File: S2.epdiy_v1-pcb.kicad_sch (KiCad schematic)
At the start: 80 parts, among them J1 USB_C_Receptacle_USB2.0, J2 Jack-DC, P1 CONN_02X13, SW1 RESET, SW2 BOOT, U1 MCP1700-1202E_SOT23, U11 TP4056, U2 ESP32-S2-WROVER, U3 TPS651851RSLR, U6 ED060XC5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

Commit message: DRC passes
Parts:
- added H1, H2, H3, H4: MountingHole, MountingHole:MountingHole_2.5mm, symbol Mechanical:MountingHole
- U3: value TPS651851RSLR -> QFN50P700X700X100-49N; footprint footprint:TPS651851RSLR -> footprint:TPS65185RGZR_700X700X100-49N
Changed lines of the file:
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@@
       (effects (font (size 1.524 1.524)))
     )
-    (property "Value" "TPS651851RSLR" (id 1) (at 290.83 147.8026 0)
+    (property "Value" "QFN50P700X700X100-49N" (id 1) (at 290.83 147.8026 0)
       (effects (font (size 1.524 1.524)))
     )
-    (property "Footprint" "footprint:TPS651851RSLR" (id 2) (at 276.86 148.844 0)
+    (property "Footprint" "footprint:TPS65185RGZR_700X700X100-49N" (id 2) (at 276.86 148.844 0)
       (effects (font (size 1.524 1.524)) hide)
     )
@@
     (pin "9")
   )
+  (symbol (lib_id "Mechanical:MountingHole") (at 246.38 260.35 0) (unit 1)
+    (in_bom yes) (on_board yes) (fields_autoplaced)
+    (property "Reference" "H4" (id 0) (at 248.92 259.4415 0)
+      (effects (font (size 1.27 1.27)) (justify left))
+    )
+    (property "Value" "MountingHole" (id 1) (at 248.92 262.2166 0)
+      (effects (font (size 1.27 1.27)) (justify left))
+    )
+    (property "Footprint" "MountingHole:MountingHole_2.5mm" (id 2) (at 246.38 260.35 0)
+      (effects (font (size 1.27 1.27)) hide)
+    )
+    (property "Datasheet" "~" (id 3) (at 246.38 260.35 0)
+      (effects (font (size 1.27 1.27)) hide)
+    )
+  )
   (symbol (lib_id "Device:R") (at 80.01 40.64 270) (unit 1)
     (in_bom yes) (on_board yes)
@@
     (pin "1")
   )
+  (symbol (lib_id "Mechanical:MountingHole") (at 228.6 260.35 0) (unit 1)
+    (in_bom yes) (on_board yes) (fields_autoplaced)
+    (property "Reference" "H2" (id 0) (at 231.14 259.4415 0)
+      (effects (font (size 1.27 1.27)) (justify left))
+    )
+    (property "Value" "MountingHole" (id 1) (at 231.14 262.2166 0)
+      (effects (font (size 1.27 1.27)) (justify left))
+    )
+    (property "Footprint" "MountingHole:MountingHole_2.5mm" (id 2) (at 228.6 260.35 0)
+      (effects (font (size 1.27 1.27)) hide)
+    )
+    (property "Datasheet" "~" (id 3) (at 228.6 260.35 0)
+      (effects (font (size 1.27 1.27)) hide)
+    )
+  )
   (symbol (lib_id "Device:R") (at 334.01 82.55 0) (unit 1)
     (in_bom yes) (on_board yes) (fields_autoplaced)
@@
     (pin "1")
     (pin "2")
+  )
+  (symbol (lib_id "Mechanical:MountingHole") (at 228.6 255.27 0) (unit 1)
+    (in_bom yes) (on_board yes) (fields_autoplaced)
+    (property "Reference" "H1" (id 0) (at 231.14 254.3615 0)
+      (effects (font (size 1.27 1.27)) (justify left))
+    )
+    (property "Value" "MountingHole" (id 1) (at 231.14 257.1366 0)
+      (effects (font (size 1.27 1.27)) (justify left))
+    )
+    (property "Footprint" "MountingHole:MountingHole_2.5mm" (id 2) (at 228.6 255.27 0)
+      (effects (font (size 1.27 1.27)) hide)
+    )
+    (property "Datasheet" "~" (id 3) (at 228.6 255.27 0)
+      (effects (font (size 1.27 1.27)) hide)
+    )
+  )
+  (symbol (lib_id "Mechanical:MountingHole") (at 246.38 255.27 0) (unit 1)
+    (in_bom yes) (on_board yes) (fields_autoplaced)
+    (property "Reference" "H3" (id 0) (at 248.92 254.3615 0)
+      (effects (font (size 1.27 1.27)) (justify left))
+    )
+    (property "Value" "MountingHole" (id 1) (at 248.92 257.1366 0)
+      (effects (font (size 1.27 1.27)) (justify left))
+    )
+    (property "Footprint" "MountingHole:MountingHole_2.5mm" (id 2) (at 246.38 255.27 0)
+      (effects (font (size 1.27 1.27)) hide)
+    )
+    (property "Datasheet" "~" (id 3) (at 246.38 255.27 0)
+      (effects (font (size 1.27 1.27)) hide)
+    )
   )
   (symbol (lib_id "Device:C") (at 325.12 53.34 180) (unit 1)
@@
       (reference "D9") (unit 1) (value "RED") (footprint "LED_SMD:LED_0805_2012Metric")
     )
+    (path "/c17299c3-8f60-4082-9be0-bbabc66e38fd"
+      (reference "H1") (unit 1) (value "MountingHole") (footprint "MountingHole:MountingHole_2.5mm")
+    )
+    (path "/ad47bbf2-3f06-4e1b-a037-d0ec556dc5e1"
+      (reference "H2") (unit 1) (value "MountingHole") (footprint "MountingHole:MountingHole_2.5mm")
+    )
+    (path "/c31da7ac-0e84-49c9-a671-1085a8d3b053"
+      (reference "H3") (unit 1) (value "MountingHole") (footprint "MountingHole:MountingHole_2.5mm")
+    )
+    (path "/693f52c8-d32f-4dba-8081-49f9b563b51a"
+      (reference "H4") (unit 1) (value "MountingHole") (footprint "MountingHole:MountingHole_2.5mm")
+    )
     (path "/a74e1b96-4789-49e0-832a-03b096a8ecaa"
       (reference "J1") (unit 1) (value "USB_C_Receptacle_USB2.0") (footprint "footprint:USB_C_Receptacle_HRO_TYPE-C-31-M-12")
@@
     )
     (path "/00000000-0000-0000-0000-0000607396d1"
-      (reference "U3") (unit 1) (value "TPS651851RSLR") (footprint "footprint:TPS651851RSLR")
+      (reference "U3") (unit 1) (value "QFN50P700X700X100-49N") (footprint "footprint:TPS65185RGZR_700X700X100-49N")
     )
     (path "/00000000-0000-0000-0000-000061320af7"

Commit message: Passes DRC
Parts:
- added TP33: TestPoint, TestPoint:TestPoint_Pad_2.0x2.0mm, symbol Connector:TestPoint
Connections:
- net EPD_VDD: now also TP33.1
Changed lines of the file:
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@@
   (junction (at 321.31 232.41) (diameter 0) (color 0 0 0 0)
   )
+  (junction (at 360.68 161.29) (diameter 0) (color 0 0 0 0)
+  )
   (no_connect (at 378.46 41.91))
   (no_connect (at 102.87 138.43))
@@
     (stroke (width 0) (type default) (color 0 0 0 0))
   )
+  (wire (pts (xy 360.68 161.29) (xy 312.42 161.29))
+    (stroke (width 0) (type default) (color 0 0 0 0))
+  )
   (wire (pts (xy 151.13 210.82) (xy 144.78 210.82))
     (stroke (width 0) (type default) (color 0 0 0 0))
@@
     (stroke (width 0) (type default) (color 0 0 0 0))
   )
+  (wire (pts (xy 312.42 162.56) (xy 300.99 162.56))
+    (stroke (width 0) (type default) (color 0 0 0 0))
+  )
   (wire (pts (xy 250.19 200.66) (xy 243.84 200.66))
     (stroke (width 0) (type default) (color 0 0 0 0))
@@
     (stroke (width 0) (type default) (color 0 0 0 0))
   )
+  (wire (pts (xy 361.95 161.29) (xy 360.68 161.29))
+    (stroke (width 0) (type default) (color 0 0 0 0))
+  )
   (wire (pts (xy 300.99 157.48) (xy 308.61 157.48))
     (stroke (width 0) (type default) (color 0 0 0 0))
@@
     (stroke (width 0) (type default) (color 0 0 0 0))
   )
+  (wire (pts (xy 312.42 161.29) (xy 312.42 162.56))
+    (stroke (width 0) (type default) (color 0 0 0 0))
+  )
   (wire (pts (xy 331.47 41.91) (xy 331.47 49.53))
     (stroke (width 0) (type default) (color 0 0 0 0))
@@
     (effects (font (size 1.27 1.27)) (justify right bottom))
   )
-  (global_label "EPD_VDD" (shape input) (at 300.99 162.56 0) (fields_autoplaced)
+  (global_label "EPD_VDD" (shape input) (at 361.95 161.29 0) (fields_autoplaced)
     (effects (font (size 1.27 1.27)) (justify left))
-    (property "Intersheet References" "${INTERSHEET_REFS}" (id 0) (at -34.29 0 0)
+    (property "Intersheet References" "${INTERSHEET_REFS}" (id 0) (at 26.67 -1.27 0)
       (effects (font (size 1.27 1.27)) hide)
     )
@@
     (pin "9")
   )
+  (symbol (lib_id "Connector:TestPoint") (at 360.68 161.29 0) (unit 1)
+    (in_bom yes) (on_board yes)
+    (property "Reference" "TP33" (id 0) (at 359.41 156.21 0)
+      (effects (font (size 1.27 1.27)) (justify left))
+    )
+    (property "Value" "TestPoint" (id 1) (at 363.22 156.21 0)
+      (effects (font (size 1.27 1.27)) (justify left))
+    )
+    (property "Footprint" "TestPoint:TestPoint_Pad_2.0x2.0mm" (id 2) (at 365.76 161.29 0)
+      (effects (font (size 1.27 1.27)) hide)
+    )
+    (property "Datasheet" "~" (id 3) (at 365.76 161.29 0)
+      (effects (font (size 1.27 1.27)) hide)
+    )
+    (pin "1")
+  )
   (symbol (lib_id "Device:LED") (at 326.39 74.93 90) (unit 1)
     (in_bom yes) (on_board yes) (fields_autoplaced)
@@
       (reference "TP5") (unit 1) (value "VCOM") (footprint "TestPoint:TestPoint_Pad_D2.5mm")
     )
+    (path "/de954fc5-54aa-4912-850f-059c315d7062"
+      (reference "TP33") (unit 1) (value "TestPoint") (footprint "TestPoint:TestPoint_Pad_2.0x2.0mm")
+    )
     (path "/6f2dad6e-4f7a-4655-bd41-70ba0551820e"

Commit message: LCSC
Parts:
- C14: LCSC (none) -> C28323
- D8: LCSC (none) -> C2297
- D9: LCSC (none) -> C84256
- R2, R3: value 1K -> 2K2; LCSC (none) -> C25804
- R6, R7: LCSC (none) -> C25803
- SW2: LCSC (none) -> C202388
- U11: LCSC (none) -> C16581
- U2: LCSC (none) -> C701333
- U7: value TPS2113APW -> TPS2113APWR; LCSC (none) -> C130052
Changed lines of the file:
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@@
+      (effects (font (size 1.27 1.27)) hide)
+    )
+    (property "LCSC" "C84256" (id 4) (at 334.01 74.93 90)
       (effects (font (size 1.27 1.27)) hide)
     )
@@
       (effects (font (size 1.524 1.524)))
     )
-    (property "Value" "TPS2113APW" (id 1) (at 360.68 30.5235 0)
+    (property "Value" "TPS2113APWR" (id 1) (at 360.68 30.5235 0)
       (effects (font (size 1.524 1.524)))
     )
@@
     (property "Datasheet" "" (id 3) (at 360.68 44.45 0)
       (effects (font (size 1.524 1.524)))
+    )
+    (property "LCSC" "C130052" (id 4) (at 360.68 44.45 0)
+      (effects (font (size 1.27 1.27)) hide)
     )
     (pin "1")
@@
       (effects (font (size 1.27 1.27)) hide)
     )
+    (property "LCSC" "C28323" (id 4) (at 229.87 49.53 0)
+      (effects (font (size 1.27 1.27)) hide)
+    )
     (pin "1")
     (pin "2")
@@
     )
     (property "Datasheet" "https://www.espressif.com/sites/default/files/documentation/esp32-s2-wroom_esp32-s2-wroom-i_datasheet_en.pdf" (id 3) (at 139.7 45.72 0)
+      (effects (font (size 1.27 1.27)) hide)
+    )
+    (property "LCSC" "C701333" (id 4) (at 132.08 66.04 0)
       (effects (font (size 1.27 1.27)) hide)
     )
@@
       (effects (font (size 1.27 1.27)) hide)
     )
+    (property "LCSC" "C25803" (id 4) (at 80.01 40.64 90)
+      (effects (font (size 1.27 1.27)) hide)
+    )
     (pin "1")
     (pin "2")
@@
       (effects (font (size 1.27 1.27)) (justify left))
     )
-    (property "Value" "1K" (id 1) (at 335.788 84.4166 0)
+    (property "Value" "2K2" (id 1) (at 335.788 84.4166 0)
       (effects (font (size 1.27 1.27)) (justify left))
     )
@@
     )
     (property "Datasheet" "~" (id 3) (at 334.01 82.55 0)
+      (effects (font (size 1.27 1.27)) hide)
+    )
+    (property "LCSC" "C25804" (id 4) (at 334.01 82.55 0)
       (effects (font (size 1.27 1.27)) hide)
     )
@@
     (property "Datasheet" "" (id 3) (at 361.95 85.09 0)
       (effects (font (size 1.524 1.524)))
+    )
+    (property "LCSC" "C16581" (id 4) (at 361.95 85.09 0)
+      (effects (font (size 1.27 1.27)) hide)
     )
     (pin "1")
@@
       (effects (font (size 1.27 1.27)) hide)
     )
+    (property "LCSC" "C2297" (id 4) (at 326.39 74.93 90)
+      (effects (font (size 1.27 1.27)) hide)
+    )
     (pin "1")
     (pin "2")
@@
       (effects (font (size 1.27 1.27)) hide)
     )
-    (property "Datasheet" "~" (id 3) (at 237.49 36.83 0)
+    (property "Datasheet" "" (id 3) (at 237.49 36.83 0)
+      (effects (font (size 1.27 1.27)) hide)
+    )
+    (property "LCSC" "C202388" (id 4) (at 237.49 41.91 0)
       (effects (font (size 1.27 1.27)) hide)
     )
@@
       (effects (font (size 1.27 1.27)) hide)
     )
+    (property "LCSC" "C25803" (id 4) (at 80.01 43.18 90)
+      (effects (font (size 1.27 1.27)) hide)
+    )
     (pin "1")
     (pin "2")
@@
       (effects (font (size 1.27 1.27)) (justify left))
     )
-    (property "Value" "1K" (id 1) (at 328.168 84.4166 0)
+    (property "Value" "2K2" (id 1) (at 328.168 84.4166 0)
       (effects (font (size 1.27 1.27)) (justify left))
     )
@@
     )
     (property "Datasheet" "~" (id 3) (at 326.39 82.55 0)
+      (effects (font (size 1.27 1.27)) hide)
+    )
+    (property "LCSC" "C25804" (id 4) (at 326.39 82.55 0)
       (effects (font (size 1.27 1.27)) hide)
     )
@@
     )
     (path "/f7be12b1-ea68-4680-ba6e-0b0986167f39"
-      (reference "R2") (unit 1) (value "1K") (footprint "Resistor_SMD:R_0603_1608Metric")
+      (reference "R2") (unit 1) (value "2K2") (footprint "Resistor_SMD:R_0603_1608Metric")
     )
     (path "/b392c915-b843-4114-8bca-8feaa4d154f9"
-      (reference "R3") (unit 1) (value "1K") (footprint "Resistor_SMD:R_0603_1608Metric")
+      (reference "R3") (unit 1) (value "2K2") (footprint "Resistor_SMD:R_0603_1608Metric")
     )
     (path "/468ff6b2-84c2-4c8f-aa2b-40a098fd4368"
@@
     )
     (path "/38a48d5e-8f90-4cde-a529-54b3116299fc"
-      (reference "U7") (unit 1) (value "TPS2113APW") (footprint "footprint:TPS2113APW")
+      (reference "U7") (unit 1) (value "TPS2113APWR") (footprint "footprint:TPS2113APW")
     )
     (path "/db763171-2d21-4254-a43f-5acafccd52ae"

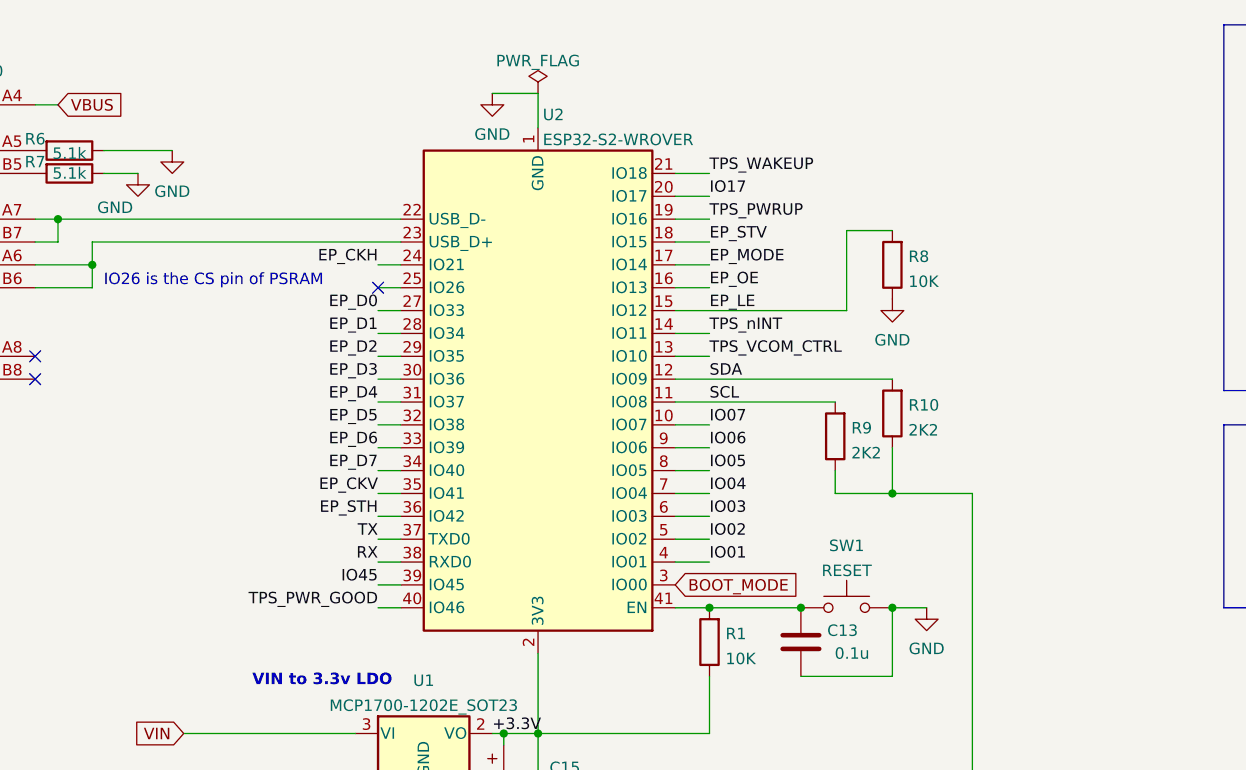
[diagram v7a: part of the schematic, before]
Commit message: 16 VNEG_IN was not connected properly
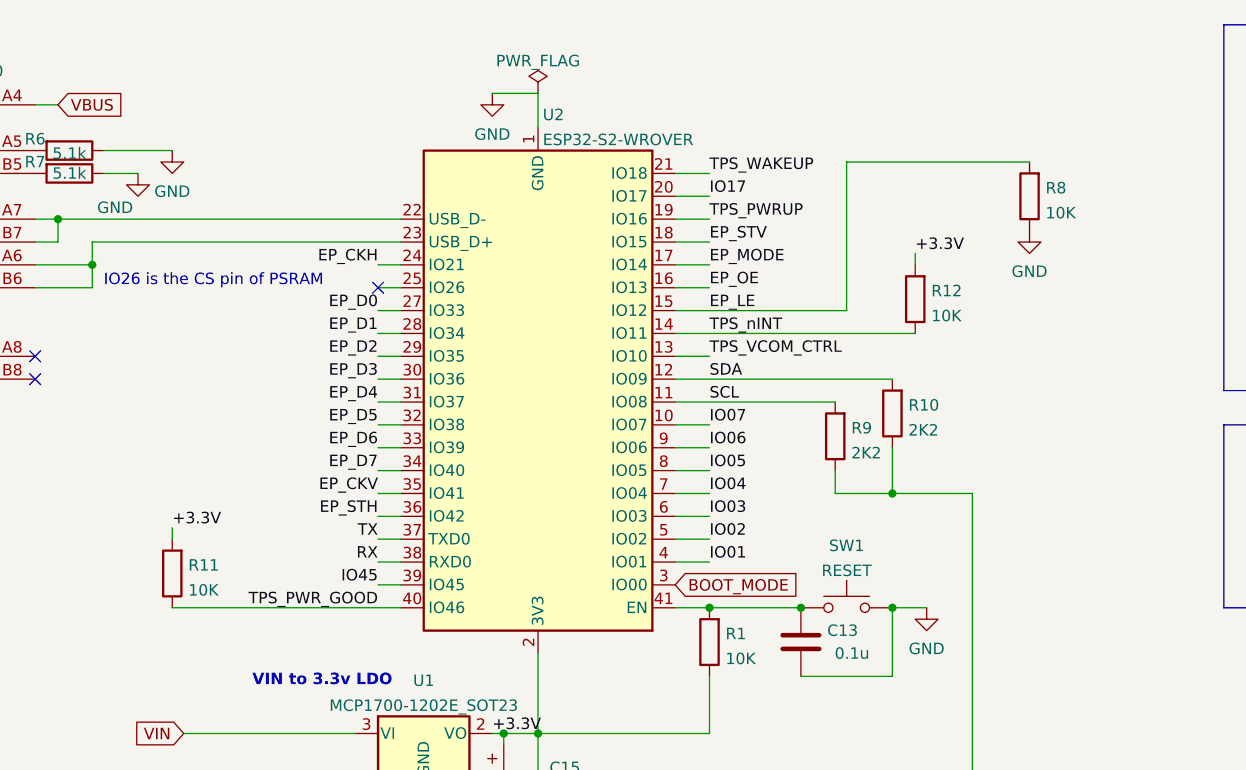
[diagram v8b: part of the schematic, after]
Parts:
- added R11, R12: 10K, Resistor_SMD:R_0603_1608Metric, symbol Device:R
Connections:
- net +3.3V: now also R11.2, R12.2
- net TPS_PWR_GOOD: now also R11.1
- net TPS_nINT: now also R12.1
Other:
- moved on the sheet: R8
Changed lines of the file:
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@@
     (stroke (width 0) (type default) (color 0 0 0 0))
   )
+  (wire (pts (xy 173.99 52.07) (xy 173.99 53.34))
+    (stroke (width 0) (type default) (color 0 0 0 0))
+  )
   (wire (pts (xy 151.13 105.41) (xy 132.08 105.41))
     (stroke (width 0) (type default) (color 0 0 0 0))
@@
     (stroke (width 0) (type default) (color 0 0 0 0))
   )
-  (wire (pts (xy 166.37 58.42) (xy 166.37 49.53))
+  (wire (pts (xy 166.37 58.42) (xy 166.37 41.91))
     (stroke (width 0) (type default) (color 0 0 0 0))
   )
@@
     (stroke (width 0) (type default) (color 0 0 0 0))
   )
-  (wire (pts (xy 151.13 60.96) (xy 147.32 60.96))
+  (wire (pts (xy 147.32 60.96) (xy 173.99 60.96))
     (stroke (width 0) (type default) (color 0 0 0 0))
   )
@@
     (stroke (width 0) (type default) (color 0 0 0 0))
   )
+  (wire (pts (xy 91.44 82.55) (xy 91.44 83.82))
+    (stroke (width 0) (type default) (color 0 0 0 0))
+  )
   (wire (pts (xy 311.15 191.77) (xy 351.79 191.77))
     (stroke (width 0) (type default) (color 0 0 0 0))
@@
     (stroke (width 0) (type default) (color 0 0 0 0))
   )
-  (wire (pts (xy 166.37 49.53) (xy 171.45 49.53))
+  (wire (pts (xy 166.37 41.91) (xy 186.69 41.91))
     (stroke (width 0) (type default) (color 0 0 0 0))
   )
@@
     (stroke (width 0) (type default) (color 0 0 0 0))
   )
-  (wire (pts (xy 114.3 91.44) (xy 116.84 91.44))
+  (wire (pts (xy 91.44 91.44) (xy 116.84 91.44))
     (stroke (width 0) (type default) (color 0 0 0 0))
   )
@@
     (effects (font (size 1.27 1.27)) (justify left bottom))
   )
+  (label "+3.3V" (at 91.44 82.55 0)
+    (effects (font (size 1.27 1.27)) (justify left bottom))
+  )
   (label "TPS_nINT" (at 151.13 60.96 0)
     (effects (font (size 1.27 1.27)) (justify left bottom))
@@
     (effects (font (size 1.27 1.27)) (justify left bottom))
   )
+  (label "+3.3V" (at 173.99 52.07 0)
+    (effects (font (size 1.27 1.27)) (justify left bottom))
+  )
   (label "EP_STH" (at 114.3 81.28 180)
     (effects (font (size 1.27 1.27)) (justify right bottom))
@@
     (pin "1")
   )
+  (symbol (lib_id "Device:R") (at 173.99 57.15 180) (unit 1)
+    (in_bom yes) (on_board yes) (fields_autoplaced)
+    (property "Reference" "R12" (id 0) (at 175.768 56.2415 0)
+      (effects (font (size 1.27 1.27)) (justify right))
+    )
+    (property "Value" "10K" (id 1) (at 175.768 59.0166 0)
+      (effects (font (size 1.27 1.27)) (justify right))
+    )
+    (property "Footprint" "Resistor_SMD:R_0603_1608Metric" (id 2) (at 175.768 57.15 90)
+      (effects (font (size 1.27 1.27)) hide)
+    )
+    (property "Datasheet" "~" (id 3) (at 173.99 57.15 0)
+      (effects (font (size 1.27 1.27)) hide)
+    )
+    (pin "1")
+    (pin "2")
+  )
   (symbol (lib_id "epd_breakout:TPS2113APW") (at 360.68 44.45 0) (unit 1)
     (in_bom yes) (on_board yes) (fields_autoplaced)
@@
     (pin "2")
   )
+  (symbol (lib_id "Device:R") (at 91.44 87.63 180) (unit 1)
+    (in_bom yes) (on_board yes) (fields_autoplaced)
+    (property "Reference" "R11" (id 0) (at 93.218 86.7215 0)
+      (effects (font (size 1.27 1.27)) (justify right))
+    )
+    (property "Value" "10K" (id 1) (at 93.218 89.4966 0)
+      (effects (font (size 1.27 1.27)) (justify right))
+    )
+    (property "Footprint" "Resistor_SMD:R_0603_1608Metric" (id 2) (at 93.218 87.63 90)
+      (effects (font (size 1.27 1.27)) hide)
+    )
+    (property "Datasheet" "~" (id 3) (at 91.44 87.63 0)
+      (effects (font (size 1.27 1.27)) hide)
+    )
+    (pin "1")
+    (pin "2")
+  )
   (symbol (lib_id "Regulator_Linear:MCP1700-1202E_SOT23") (at 119.38 105.41 0) (unit 1)
     (in_bom yes) (on_board yes) (fields_autoplaced)
@@
     (pin "1")
   )
-  (symbol (lib_id "Device:R") (at 171.45 53.34 180) (unit 1)
+  (symbol (lib_id "Device:R") (at 186.69 45.72 180) (unit 1)
     (in_bom yes) (on_board yes) (fields_autoplaced)
-    (property "Reference" "R8" (id 0) (at 173.228 52.4315 0)
+    (property "Reference" "R8" (id 0) (at 188.468 44.8115 0)
       (effects (font (size 1.27 1.27)) (justify right))
     )
-    (property "Value" "10K" (id 1) (at 173.228 55.2066 0)
+    (property "Value" "10K" (id 1) (at 188.468 47.5866 0)
       (effects (font (size 1.27 1.27)) (justify right))
     )
-    (property "Footprint" "Resistor_SMD:R_0603_1608Metric" (id 2) (at 173.228 53.34 90)
+    (property "Footprint" "Resistor_SMD:R_0603_1608Metric" (id 2) (at 188.468 45.72 90)
       (effects (font (size 1.27 1.27)) hide)
     )
-    (property "Datasheet" "~" (id 3) (at 171.45 53.34 0)
+    (property "Datasheet" "~" (id 3) (at 186.69 45.72 0)
       (effects (font (size 1.27 1.27)) hide)
     )
@@
     (pin "S1")
   )
-  (symbol (lib_id "power:GND") (at 171.45 57.15 0) (unit 1)
+  (symbol (lib_id "power:GND") (at 186.69 49.53 0) (unit 1)
     (in_bom yes) (on_board yes) (fields_autoplaced)
-    (property "Reference" "#PWR0110" (id 0) (at 171.45 63.5 0)
+    (property "Reference" "#PWR0110" (id 0) (at 186.69 55.88 0)
       (effects (font (size 1.27 1.27)) hide)
     )
-    (property "Value" "GND" (id 1) (at 171.45 61.7125 0))
-    (property "Footprint" "" (id 2) (at 171.45 57.15 0)
+    (property "Value" "GND" (id 1) (at 186.69 54.0925 0))
+    (property "Footprint" "" (id 2) (at 186.69 49.53 0)
       (effects (font (size 1.27 1.27)) hide)
     )
-    (property "Datasheet" "" (id 3) (at 171.45 57.15 0)
+    (property "Datasheet" "" (id 3) (at 186.69 49.53 0)
       (effects (font (size 1.27 1.27)) hide)
     )
@@
       (reference "R10") (unit 1) (value "2K2") (footprint "Resistor_SMD:R_0603_1608Metric")
     )
+    (path "/6ba09acc-98f1-48e4-bbc2-2b3e8d01ace7"
+      (reference "R11") (unit 1) (value "10K") (footprint "Resistor_SMD:R_0603_1608Metric")
+    )
+    (path "/300a4445-5856-49c4-bc04-ca52d68ca82b"
+      (reference "R12") (unit 1) (value "10K") (footprint "Resistor_SMD:R_0603_1608Metric")
+    )
     (path "/00000000-0000-0000-0000-00006283baac"
